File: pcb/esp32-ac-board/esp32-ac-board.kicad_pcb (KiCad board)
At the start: 2 copper layers, 88.9 x 68.6 mm, 7 parts, among them J1 Conn_01x15, J2 Conn_01x15, Q1 Q_NPN_BCE

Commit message: Fix schematic, redo PCB
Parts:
- added SW1: SW_Push, Button_Switch_THT:SW_PUSH-12mm, F.Cu at (134.0, 67.9)
- moved J1 111.8 mm to (153.7, 116.2), turned to 90 degrees
- moved R1 88.6 mm to (133.3, 108.0), turned to 90 degrees
- moved ESP32 76.9 mm to (200.0, 106.0)
- moved Q1 70.6 mm to (141.6, 95.9), turned to 90 degrees
- moved D1 70.3 mm to (143.5, 85.1), turned to 180 degrees
- moved DHT_22 68.0 mm to (138.4, 105.4)
- moved J2 40.7 mm to (189.2, 66.0), turned to 270 degrees
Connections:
- net Net-(ESP32-Pad23) renamed /5
- net Net-(ESP32-Pad8) renamed /25
- D1 pad 1: +5V -> VCC
- DHT_22 pad 1: Net-(DHT_22-Pad1) -> /3V3
- DHT_22 pad 2: Net-(DHT_22-Pad2) -> /TEMP
- ESP32 pad 1: Net-(ESP32-Pad1) -> /EN
- ESP32 pad 10: Net-(ESP32-Pad10) -> /27
- ESP32 pad 11: Net-(ESP32-Pad11) -> /TEMP
- ESP32 pad 12: Net-(ESP32-Pad12) -> /BTN
- ESP32 pad 13: Net-(DHT_22-Pad2) -> /13
- ESP32 pad 15: +5V -> VCC
- ESP32 pad 16: Net-(DHT_22-Pad1) -> /3V3
- ESP32 pad 17: Net-(ESP32-Pad17) -> GND
- ESP32 pad 18: Net-(ESP32-Pad18) -> /15
- ESP32 pad 19: Net-(ESP32-Pad19) -> /2
- ESP32 pad 2: Net-(ESP32-Pad2) -> /36
- ESP32 pad 20: Net-(ESP32-Pad20) -> /4
- ESP32 pad 21: Net-(ESP32-Pad21) -> /16
- ESP32 pad 22: Net-(ESP32-Pad22) -> /17
- ESP32 pad 24: Net-(ESP32-Pad24) -> /18
- ESP32 pad 25: Net-(ESP32-Pad25) -> /19
- ESP32 pad 26: Net-(ESP32-Pad26) -> /21
- ESP32 pad 27: Net-(ESP32-Pad27) -> /3
- ESP32 pad 28: Net-(ESP32-Pad28) -> /1
- ESP32 pad 29: Net-(ESP32-Pad29) -> /22
- ESP32 pad 3: Net-(ESP32-Pad3) -> /39
- ESP32 pad 30: Net-(ESP32-Pad30) -> /23
- ESP32 pad 4: Net-(ESP32-Pad4) -> /34
- ESP32 pad 5: Net-(ESP32-Pad5) -> /35
- ESP32 pad 6: Net-(ESP32-Pad6) -> /32
- ESP32 pad 7: Net-(ESP32-Pad7) -> /33
- ESP32 pad 9: Net-(ESP32-Pad9) -> /SEND
- J1 pad 1: +5V -> /EN
- J1 pad 10: Net-(ESP32-Pad6) -> /27
- J1 pad 11: Net-(ESP32-Pad5) -> /TEMP
- J1 pad 12: Net-(ESP32-Pad4) -> /BTN
- J1 pad 13: Net-(ESP32-Pad3) -> /13
- J1 pad 14: Net-(ESP32-Pad2) -> GND
- J1 pad 15: Net-(ESP32-Pad1) -> VCC
- J1 pad 2: GND -> /36
- J1 pad 3: Net-(DHT_22-Pad2) -> /39
- J1 pad 4: Net-(ESP32-Pad12) -> /34
- J1 pad 5: Net-(ESP32-Pad11) -> /35
- J1 pad 6: Net-(ESP32-Pad10) -> /32
- J1 pad 7: Net-(ESP32-Pad9) -> /33
- J1 pad 9: Net-(ESP32-Pad7) -> /SEND
- J2 pad 1: Net-(ESP32-Pad30) -> /3V3
- J2 pad 10: Net-(ESP32-Pad21) -> /19
- J2 pad 11: Net-(ESP32-Pad20) -> /21
- J2 pad 12: Net-(ESP32-Pad19) -> /3
- J2 pad 13: Net-(ESP32-Pad18) -> /1
- J2 pad 14: Net-(ESP32-Pad17) -> /22
- J2 pad 15: Net-(DHT_22-Pad1) -> /23
- J2 pad 2: Net-(ESP32-Pad29) -> GND
- J2 pad 3: Net-(ESP32-Pad28) -> /15
- J2 pad 4: Net-(ESP32-Pad27) -> /2
- J2 pad 5: Net-(ESP32-Pad26) -> /4
- J2 pad 6: Net-(ESP32-Pad25) -> /16
- J2 pad 7: Net-(ESP32-Pad24) -> /17
- J2 pad 9: Net-(ESP32-Pad22) -> /18
- Q1 pad 1: Net-(ESP32-Pad9) -> /SEND
- R1 pad 1: Net-(DHT_22-Pad1) -> /TEMP
- R1 pad 2: Net-(DHT_22-Pad2) -> /3V3
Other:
- board outline removed
- board text removed: "C"
- board text removed: "E"

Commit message: Use 5V signal like in https://hackaday.com/2016/11/17/creating-a-pcb-in-everything-kicad-part-1/
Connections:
- net VCC renamed +5V

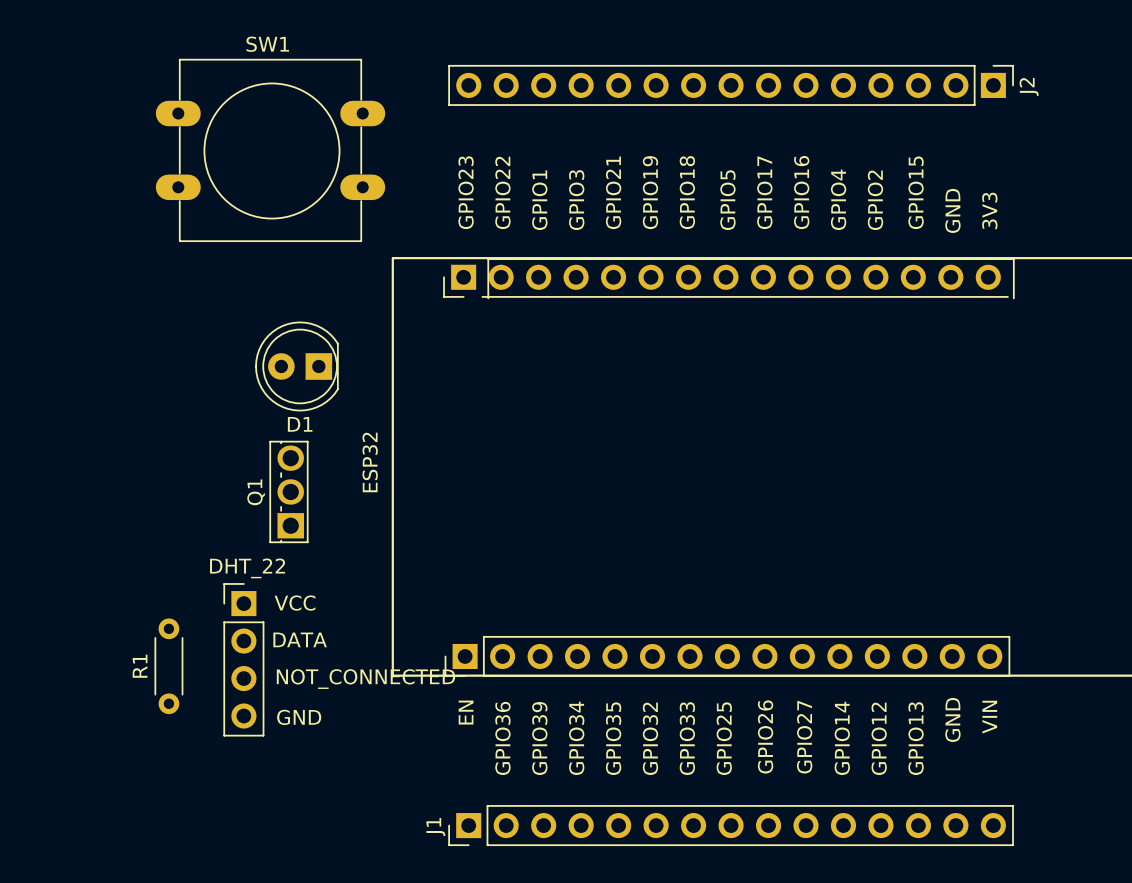
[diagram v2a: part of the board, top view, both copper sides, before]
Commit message: Add traces
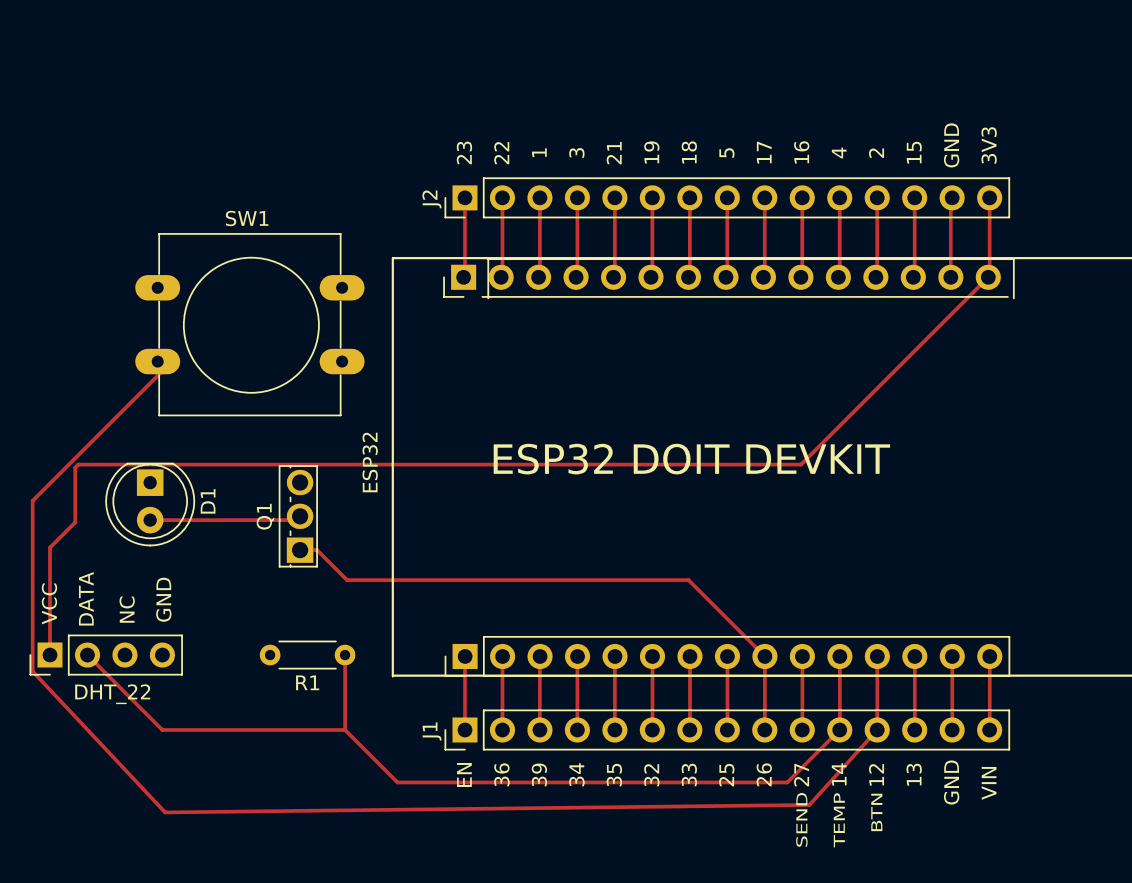
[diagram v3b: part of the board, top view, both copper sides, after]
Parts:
- D1: value LD271 -> 940nm
- R1: value R -> 10k
- moved J2 36.6 mm to (153.4, 73.7), turned to 90 degrees
- moved D1 13.9 mm to (132.1, 93.0), turned to 270 degrees
- moved R1 12.4 mm to (145.3, 104.6), turned to 180 degrees
- moved SW1 11.9 mm to (132.6, 79.8)
- moved DHT_22 8.92 mm to (129.5, 104.6), turned to 90 degrees
- moved J1 6.48 mm to (153.4, 109.7)
- moved Q1 1.77 mm to (142.2, 97.5)
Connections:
- J2 pad 1: /3V3 -> /23
- J2 pad 10: /19 -> /16
- J2 pad 11: /21 -> /4
- J2 pad 12: /3 -> /2
- J2 pad 13: /1 -> /15
- J2 pad 14: /22 -> GND
- J2 pad 15: /23 -> /3V3
- J2 pad 2: GND -> /22
- J2 pad 3: /15 -> /1
- J2 pad 4: /2 -> /3
- J2 pad 5: /4 -> /21
- J2 pad 6: /16 -> /19
- J2 pad 7: /17 -> /18
- J2 pad 9: /18 -> /17
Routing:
- net /BTN: track 0.00 -> 93.5 mm
- net /3V3: track 0.00 -> 86.1 mm
- net /TEMP: track 0.00 -> 66.1 mm
- net /SEND: track 0.00 -> 39.5 mm
- net GND: track 0.00 -> 10.4 mm
- net Net-(D1-Pad2): track 0.00 -> 10.3 mm
- net /5: track 0.00 -> 5.42 mm
- net /4: track 0.00 -> 5.42 mm
- net /3: track 0.00 -> 5.42 mm
- net /23: track 0.00 -> 5.42 mm
- net /2: track 0.00 -> 5.42 mm
- net /19: track 0.00 -> 5.42 mm
- net /18: track 0.00 -> 5.42 mm
- net /16: track 0.00 -> 5.42 mm
- net /1: track 0.00 -> 5.42 mm
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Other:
- board text added: "BTN"
- board text added: "ESP32 DOIT DEVKIT"
- board text added: "SEND"
- board text added: "TEMP"

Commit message: Copper fills
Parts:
- added ?: , , F.Cu at (156.1, 112.9)
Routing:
- added copper zone on B.Cu, net +5V
- added copper zone on F.Cu, net GND
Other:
- board outline added: 82.8 x 52.6 mm
- board text added: "www.cristiansandu.ro"
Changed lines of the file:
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@@
   (general
     (thickness 1.6)
-    (drawings 8)
+    (drawings 14)
     (tracks 83)
     (zones 0)
-    (modules 8)
+    (modules 9)
     (nets 32)
   )
@@
     (0 F.Cu signal)
     (31 B.Cu signal)
-    (32 B.Adhes user)
-    (33 F.Adhes user)
-    (34 B.Paste user)
-    (35 F.Paste user)
+    (32 B.Adhes user hide)
+    (33 F.Adhes user hide)
+    (34 B.Paste user hide)
+    (35 F.Paste user hide)
     (36 B.SilkS user)
     (37 F.SilkS user)
-    (38 B.Mask user)
-    (39 F.Mask user)
-    (40 Dwgs.User user)
-    (41 Cmts.User user)
-    (42 Eco1.User user)
-    (43 Eco2.User user)
+    (38 B.Mask user hide)
+    (39 F.Mask user hide)
+    (40 Dwgs.User user hide)
+    (41 Cmts.User user hide)
+    (42 Eco1.User user hide)
+    (43 Eco2.User user hide)
     (44 Edge.Cuts user)
-    (45 Margin user)
-    (46 B.CrtYd user)
-    (47 F.CrtYd user)
-    (48 B.Fab user)
-    (49 F.Fab user)
+    (45 Margin user hide)
+    (46 B.CrtYd user hide)
+    (47 F.CrtYd user hide)
+    (48 B.Fab user hide)
+    (49 F.Fab user hide)
   )
   (setup
@@
     (add_net "Net-(DHT_22-Pad3)")
   )
+  (module "" (layer F.Cu)
+    (at 156.083 112.903)
+    (fp_text reference "" (at 132.08 92.964) (layer F.SilkS)
+      (effects (font (size 1.27 1.27) (thickness 0.15)))
+    )
+    (fp_text value "" (at 132.08 92.964) (layer F.SilkS)
+      (effects (font (size 1.27 1.27) (thickness 0.15)))
+    )
+    (fp_text user 21 (at 132.08 92.964) (layer F.SilkS)
+      (effects (font (size 1 1) (thickness 0.15)))
+    )
+  )
   (module LED_THT:LED_D5.0mm_IRGrey (layer F.Cu)
     (at 132.08 92.964 270)
@@
       (effects (font (size 1 1) (thickness 0.15)))
     )
-    (fp_text user EN (at -6.731 -46.609 90) (layer F.SilkS)
+    (fp_text user EN (at -6.858 -46.609 90) (layer F.SilkS)
       (effects (font (size 1 1) (thickness 0.15)))
     )
@@
     )
   )
+  (gr_text "ESP32 DOIT DEVKIT" (at 168.529 91.313) (layer B.SilkS)
+    (effects (font (size 2 2) (thickness 0.15)) (justify mirror))
+  )
+  (gr_text www.cristiansandu.ro (at 130.683 117.475) (layer F.SilkS)
+    (effects (font (size 1 1) (thickness 0.15)))
+  )
+  (gr_text www.cristiansandu.ro (at 195.834 68.961) (layer B.SilkS)
+    (effects (font (size 1 1) (thickness 0.15)) (justify mirror))
+  )
+  (gr_line (start 121.666 67.183) (end 204.47 67.183) (layer Edge.Cuts) (width 0.05))
+  (gr_line (start 121.793 119.634) (end 121.666 67.183) (layer Edge.Cuts) (width 0.05))
+  (gr_line (start 204.47 119.761) (end 121.793 119.634) (layer Edge.Cuts) (width 0.05))
+  (gr_line (start 204.47 67.183) (end 204.47 119.761) (layer Edge.Cuts) (width 0.05))
   (gr_text "ESP32 DOIT DEVKIT" (at 168.656 91.44) (layer F.SilkS)
     (effects (font (size 2 2) (thickness 0.15)))
-  )
-  (gr_text "ESP32 DOIT DEVKIT" (at 168.656 91.44) (layer B.SilkS)
-    (effects (font (size 2 2) (thickness 0.15)) (justify mirror))
   )
   (gr_text BTN (at 181.356 115.316 90) (layer B.SilkS)
@@
   (segment (start 188.985 109.719) (end 188.976 109.728) (width 0.25) (layer F.Cu) (net 31))
   (segment (start 188.985 104.745) (end 188.985 109.719) (width 0.25) (layer F.Cu) (net 31))
+  (zone (net 31) (net_name +5V) (layer B.Cu) (hatch edge 0.508)
+    (connect_pads (clearance 0.508))
+    (min_thickness 0.254)
+    (fill yes (arc_segments 32) (thermal_gap 0.508) (thermal_bridge_width 0.508))
+    (polygon
+      (pts
+        (xy 122.047 67.183) (xy 204.216 67.056) (xy 204.216 119.634) (xy 121.666 119.634)
+      )
+    )
+  )
+  (zone (net 5) (net_name GND) (layer F.Cu) (hatch edge 0.508)
+    (connect_pads (clearance 0.508))
+    (min_thickness 0.254)
+    (fill yes (arc_segments 32) (thermal_gap 0.508) (thermal_bridge_width 0.508))
+    (polygon
+      (pts
+        (xy 121.539 67.31) (xy 204.597 67.31) (xy 204.343 120.015) (xy 121.412 120.015)
+      )
+    )
+  )
 )

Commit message: GERBERs
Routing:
- net GND: track 10.4 -> 48.9 mm
- net /3V3: track 86.1 -> 105.7 mm
- net /BTN: track 93.5 -> 106.0 mm
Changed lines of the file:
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@@
     (thickness 1.6)
     (drawings 14)
-    (tracks 83)
+    (tracks 101)
     (zones 0)
     (modules 9)
@@
     (0 F.Cu signal)
     (31 B.Cu signal)
-    (32 B.Adhes user hide)
-    (33 F.Adhes user hide)
+    (32 B.Adhes user)
+    (33 F.Adhes user)
     (34 B.Paste user hide)
-    (35 F.Paste user hide)
+    (35 F.Paste user)
     (36 B.SilkS user)
     (37 F.SilkS user)
-    (38 B.Mask user hide)
-    (39 F.Mask user hide)
-    (40 Dwgs.User user hide)
-    (41 Cmts.User user hide)
-    (42 Eco1.User user hide)
-    (43 Eco2.User user hide)
+    (38 B.Mask user)
+    (39 F.Mask user)
+    (40 Dwgs.User user)
+    (41 Cmts.User user)
+    (42 Eco1.User user)
+    (43 Eco2.User user)
     (44 Edge.Cuts user)
-    (45 Margin user hide)
-    (46 B.CrtYd user hide)
-    (47 F.CrtYd user hide)
-    (48 B.Fab user hide)
-    (49 F.Fab user hide)
+    (45 Margin user)
+    (46 B.CrtYd user)
+    (47 F.CrtYd user)
+    (48 B.Fab user)
+    (49 F.Fab user)
   )
   (setup
@@
       (outputformat 1)
       (mirror false)
-      (drillshape 1)
+      (drillshape 0)
       (scaleselection 1)
-      (outputdirectory ""))
+      (outputdirectory "GERBER/"))
   )
   (net 0 "")
@@
   (segment (start 125.29 104.648) (end 125.29 97.368998) (width 0.25) (layer F.Cu) (net 2))
   (segment (start 125.29 97.368998) (end 127 95.658998) (width 0.25) (layer F.Cu) (net 2))
+  (segment (start 140.208 104.648) (end 140.208 101.727) (width 0.25) (layer F.Cu) (net 2))
+  (segment (start 135.849998 97.368998) (end 125.29 97.368998) (width 0.25) (layer F.Cu) (net 2))
+  (segment (start 140.208 101.727) (end 135.849998 97.368998) (width 0.25) (layer F.Cu) (net 2))
   (segment (start 178.825 109.719) (end 178.816 109.728) (width 0.25) (layer F.Cu) (net 3))
   (segment (start 178.825 104.745) (end 178.825 109.719) (width 0.25) (layer F.Cu) (net 3))
@@
   (segment (start 186.445 109.719) (end 186.436 109.728) (width 0.25) (layer F.Cu) (net 5))
   (segment (start 186.445 104.745) (end 186.445 109.719) (width 0.25) (layer F.Cu) (net 5))
+  (segment (start 133.935001 105.673001) (end 133.759999 105.497999) (width 0.25) (layer F.Cu) (net 5))
+  (segment (start 133.759999 105.497999) (end 132.91 104.648) (width 0.25) (layer F.Cu) (net 5))
+  (segment (start 140.700001 105.673001) (end 133.935001 105.673001) (width 0.25) (layer F.Cu) (net 5))
+  (segment (start 141.233001 102.115591) (end 141.233001 105.140001) (width 0.25) (layer F.Cu) (net 5))
+  (segment (start 131.335989 96.918989) (end 136.036399 96.918989) (width 0.25) (layer F.Cu) (net 5))
+  (segment (start 130.854999 96.437999) (end 131.335989 96.918989) (width 0.25) (layer F.Cu) (net 5))
+  (segment (start 130.854999 94.915999) (end 130.854999 96.437999) (width 0.25) (layer F.Cu) (net 5))
+  (segment (start 131.491999 94.278999) (end 130.854999 94.915999) (width 0.25) (layer F.Cu) (net 5))
+  (segment (start 140.875751 94.278999) (end 131.491999 94.278999) (width 0.25) (layer F.Cu) (net 5))
+  (segment (start 141.233001 105.140001) (end 140.700001 105.673001) (width 0.25) (layer F.Cu) (net 5))
+  (segment (start 142.19875 92.956) (end 140.875751 94.278999) (width 0.25) (layer F.Cu) (net 5))
+  (segment (start 136.036399 96.918989) (end 141.233001 102.115591) (width 0.25) (layer F.Cu) (net 5))
+  (segment (start 142.24 92.956) (end 142.19875 92.956) (width 0.25) (layer F.Cu) (net 5))
   (segment (start 183.896 78.954) (end 183.805 79.045) (width 0.25) (layer F.Cu) (net 6))
   (segment (start 183.896 73.66) (end 183.896 78.954) (width 0.25) (layer F.Cu) (net 6))
@@
   (segment (start 124.114999 94.196591) (end 124.114999 105.758001) (width 0.25) (layer F.Cu) (net 20))
   (segment (start 133.55559 84.756) (end 124.114999 94.196591) (width 0.25) (layer F.Cu) (net 20))
+  (segment (start 143.314 84.756) (end 132.588 84.756) (width 0.25) (layer F.Cu) (net 20))
+  (segment (start 145.088 84.756) (end 143.314 84.756) (width 0.25) (layer F.Cu) (net 20))
   (segment (start 176.285 109.719) (end 176.276 109.728) (width 0.25) (layer F.Cu) (net 21))
   (segment (start 176.285 104.745) (end 176.285 109.719) (width 0.25) (layer F.Cu) (net 21))

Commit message: Attempt at logo
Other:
- board text added: "ESP Home Monitor v0.1"
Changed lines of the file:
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@@
   (general
     (thickness 1.6)
-    (drawings 14)
+    (drawings 15)
     (tracks 101)
     (zones 0)
@@
   (page A4)
   (layers
-    (0 F.Cu signal)
-    (31 B.Cu signal)
+    (0 F.Cu signal hide)
+    (31 B.Cu signal hide)
     (32 B.Adhes user)
     (33 F.Adhes user)
-    (34 B.Paste user hide)
+    (34 B.Paste user)
     (35 F.Paste user)
     (36 B.SilkS user)
-    (37 F.SilkS user)
+    (37 F.SilkS user hide)
     (38 B.Mask user)
     (39 F.Mask user)
@@
     )
   )
+  (gr_text "ESP Home Monitor v0.1" (at 136.525 117.348) (layer B.SilkS)
+    (effects (font (size 1.5 1.5) (thickness 0.3)) (justify mirror))
+  )
   (gr_text "ESP32 DOIT DEVKIT" (at 168.529 91.313) (layer B.SilkS)
     (effects (font (size 2 2) (thickness 0.15)) (justify mirror))
@@
     (effects (font (size 2 2) (thickness 0.15)))
   )
-  (gr_text BTN (at 181.356 115.316 90) (layer B.SilkS)
+  (gr_text BTN (at 181.356 113.411 90) (layer B.SilkS)
     (effects (font (size 0.75 1) (thickness 0.15)) (justify mirror))
   )
-  (gr_text TEMP (at 178.816 115.824 90) (layer B.SilkS)
+  (gr_text TEMP (at 179.07 114.046 90) (layer B.SilkS)
     (effects (font (size 0.75 1) (thickness 0.15)) (justify mirror))
   )
-  (gr_text SEND (at 176.276 115.824 90) (layer B.SilkS)
+  (gr_text SEND (at 176.276 114.046 90) (layer B.SilkS)
     (effects (font (size 0.75 1) (thickness 0.15)) (justify mirror))
   )

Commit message: fix logo
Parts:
- added LOGO: LOGO, ESP32:Logo, B.Cu at (138.4, 110.5)

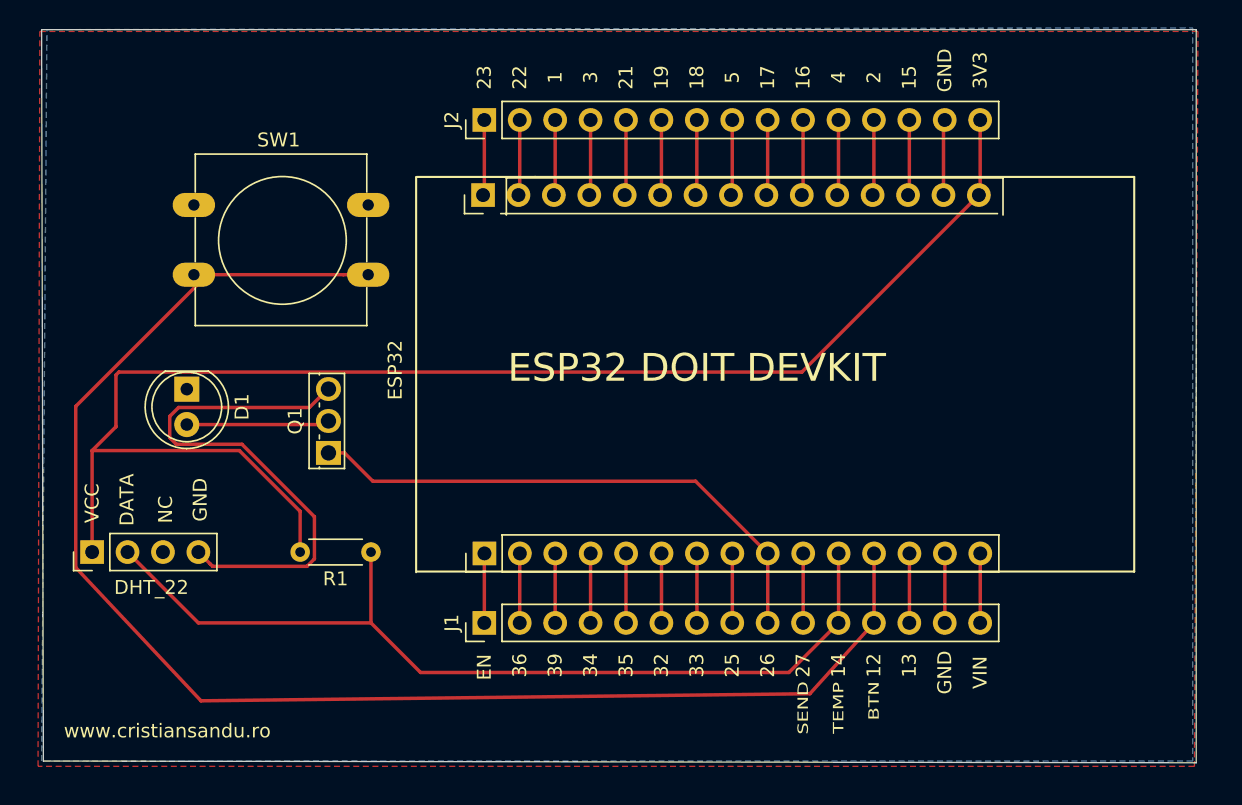
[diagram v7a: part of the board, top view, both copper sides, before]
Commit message: add screw terminal for power
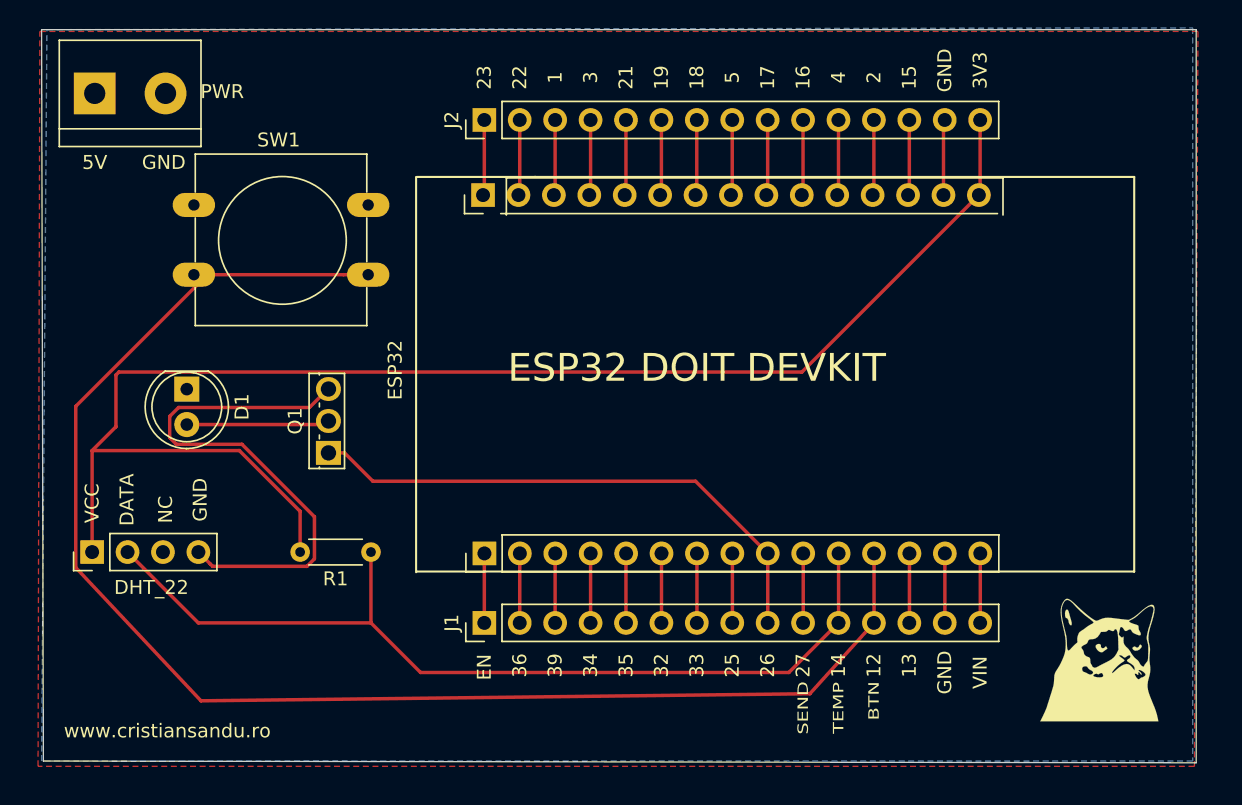
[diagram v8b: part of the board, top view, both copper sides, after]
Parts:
- added G***: LOGO, ESP32:Logo, F.Cu at (197.5, 112.0)
- added PWR: Screw_Terminal_01x02, TerminalBlock:TerminalBlock_bornier-2_P5.08mm, F.Cu at (125.5, 71.8)
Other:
- board text added: "5V"
- board text added: "GND"
